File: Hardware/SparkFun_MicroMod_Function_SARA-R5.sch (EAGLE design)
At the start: 93 parts, among them J1 MICROMOD_FUNCTION_STANDARD, J2 U.FL, J4 U.FL, J9 NANO_SIM, Q2 310mA/60V/1.6Ω, Q3 310mA/60V/1.6Ω, Q5 310mA/60V/1.6Ω, Q6 310mA/60V/1.6Ω, U1 SARA-R510M8S, U11 74HC1G04, U2 SN74AVC4T774PW, U3 3.3V, U4 EEPROM, U5 AP7361C-33FGE

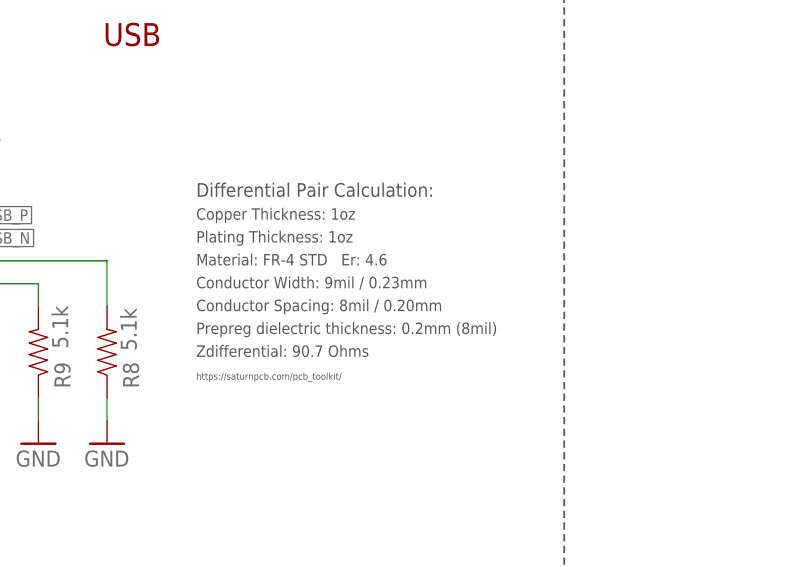
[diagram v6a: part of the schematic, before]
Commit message: USB lines updated for correct impedance calcs
-updated trace width and spacing to hit a 90 ohm differential impedance on D+/D-
-updated calculation text paragraph in SCH
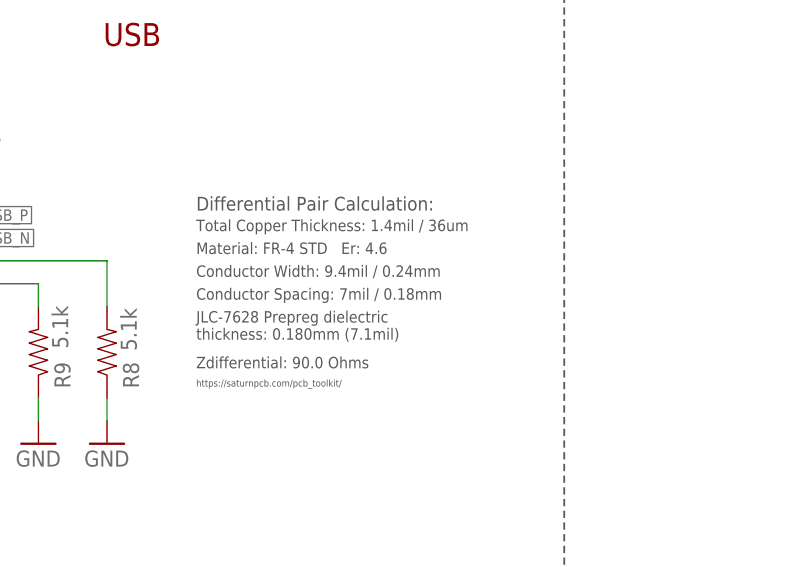
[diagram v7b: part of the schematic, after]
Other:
- note added: "Conductor Spacing: 7mil / 0.18mm"
- note added: "Conductor Width: 9.4mil / 0.24mm"
- note added: "JLC-7628 Prepreg dielectric thickness: 0.180mm (7.1mil)"
- note added: "Total Copper Thickness: 1.4mil / 36um"
- note added: "Zdifferential: 90.0 Ohms"
- note removed: "Conductor Spacing: 8mil / 0.20mm"
- note removed: "Conductor Width: 9mil / 0.23mm"
- note removed: "Copper Thickness: 1oz"
- note removed: "Plating Thickness: 1oz"
- note removed: "Prepreg dielectric thickness: 0.2mm (8mil)"
- note removed: "Zdifferential: 90.7 Ohms"
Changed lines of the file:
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@@
 <clearance class="3" value="0.1778"/>
 </class>
-<class number="4" name="DiffPair" width="0.2286" drill="0">
-<clearance class="4" value="0.2032"/>
+<class number="4" name="DiffPair" width="0.24" drill="0">
+<clearance class="4" value="0.1778"/>
 </class>
 </classes>
@@
 <text x="241.3" y="182.88" size="2.54" layer="97" font="vector">50Ω</text>
 <wire x1="330.2" y1="35.56" x2="330.2" y2="78.74" width="0.2032" layer="97" style="longdash"/>
-<text x="180.086" y="136.652" size="1.27" layer="97" font="vector">Plating Thickness: 1oz</text>
-<text x="180.086" y="134.112" size="1.27" layer="97" font="vector">Material: FR-4 STD   Er: 4.6</text>
-<text x="180.086" y="139.192" size="1.27" layer="97" font="vector">Copper Thickness: 1oz</text>
-<text x="180.086" y="129.032" size="1.27" layer="97" font="vector">Conductor Spacing: 8mil / 0.20mm</text>
-<text x="180.086" y="131.572" size="1.27" layer="97" font="vector">Conductor Width: 9mil / 0.23mm</text>
-<text x="180.086" y="126.492" size="1.27" layer="97" font="vector">Prepreg dielectric thickness: 0.2mm (8mil)</text>
-<text x="180.086" y="121.412" size="0.762" layer="97" font="vector">https://saturnpcb.com/pcb_toolkit/</text>
-<text x="180.086" y="141.732" size="1.524" layer="97" font="vector" ratio="15">Differential Pair Calculation:</text>
-<text x="180.086" y="123.952" size="1.27" layer="97" font="vector">Zdifferential: 90.7 Ohms</text>
+<text x="180.086" y="136.652" size="1.27" layer="97" font="vector"></text>
+<text x="180.086" y="136.652" size="1.27" layer="97" font="vector" align="top-left">Material: FR-4 STD   Er: 4.6</text>
+<text x="180.086" y="139.192" size="1.27" layer="97" font="vector" align="top-left">Total Copper Thickness: 1.4mil / 36um</text>
+<text x="180.086" y="131.572" size="1.27" layer="97" font="vector" align="top-left">Conductor Spacing: 7mil / 0.18mm</text>
+<text x="180.086" y="134.112" size="1.27" layer="97" font="vector" align="top-left">Conductor Width: 9.4mil / 0.24mm</text>
+<text x="180.086" y="129.032" size="1.27" layer="97" font="vector" align="top-left">JLC-7628 Prepreg dielectric
+thickness: 0.180mm (7.1mil)</text>
+<text x="180.086" y="121.412" size="0.762" layer="97" font="vector" align="top-left">https://saturnpcb.com/pcb_toolkit/</text>
+<text x="180.086" y="141.732" size="1.524" layer="97" font="vector" ratio="15" align="top-left">Differential Pair Calculation:</text>
+<text x="180.086" y="123.952" size="1.27" layer="97" font="vector" align="top-left">Zdifferential: 90.0 Ohms</text>
 <text x="139.7" y="88.9" size="2.032" layer="97" font="vector" rot="MR180" align="top-left">USB_SHLD Jumper
 Use this jumper to connect/disconnect

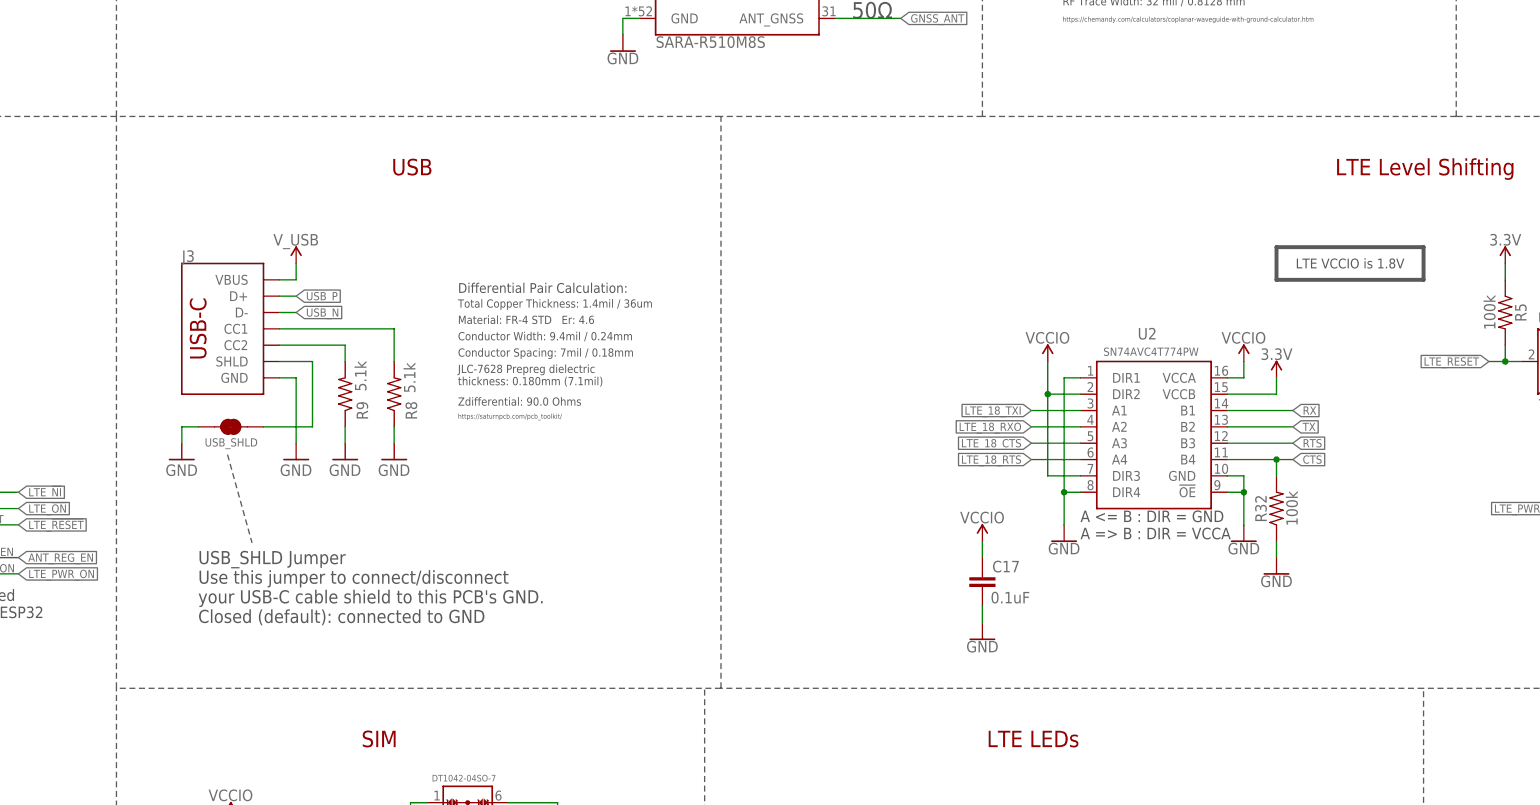
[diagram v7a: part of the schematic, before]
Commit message: ESD diode on D+ and D- USB lines
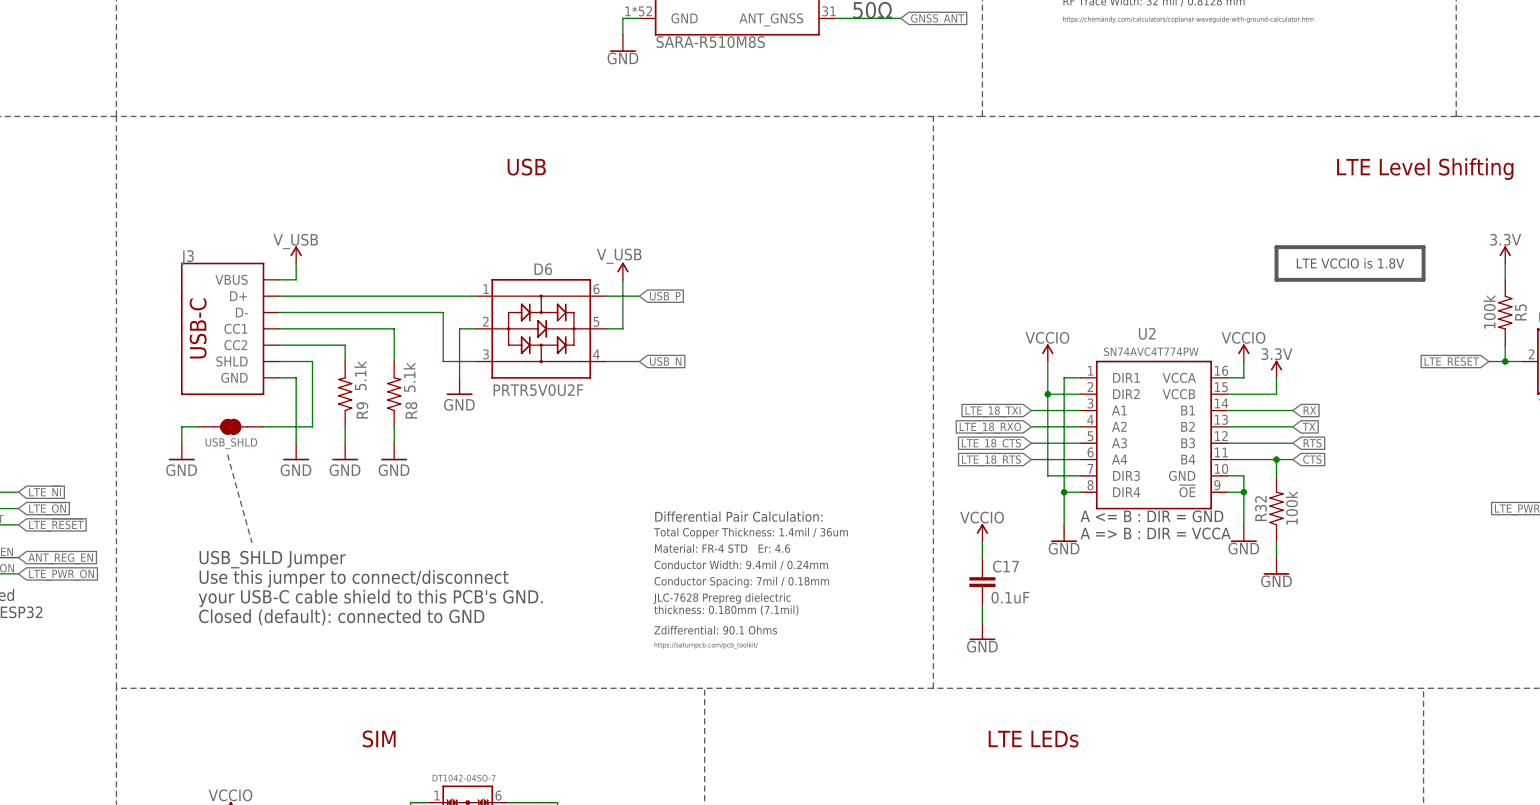
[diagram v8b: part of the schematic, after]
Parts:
- added D6: PRTR5V0U2F, SparkFun-IC-Power:PRTR5V0U2F
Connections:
- new net N$10: D6.1, J3.D+
- new net N$15: D6.3, J3.D-
- net GND: now also D6.2
- net USB_N: now also D6.4; no longer J3.D-
- net USB_P: now also D6.6; no longer J3.D+
- net V_USB: now also D6.5
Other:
- note added: "Zdifferential: 90.1 Ohms"
- note removed: "Zdifferential: 90.0 Ohms"
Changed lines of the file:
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@@
 <part name="GND25" library="SparkFun-PowerSymbols" deviceset="GND" device=""/>
 <part name="GND26" library="SparkFun-PowerSymbols" deviceset="GND" device=""/>
+<part name="GND27" library="SparkFun-PowerSymbols" deviceset="GND" device=""/>
+<part name="D6" library="SparkFun-IC-Power" deviceset="PRTR5V0U2" device="F"/>
+<part name="SUPPLY21" library="SparkFun-PowerSymbols" deviceset="V_USB" device=""/>
 </parts>
 <sheets>
@@
 <text x="274.066" y="182.372" size="0.762" layer="97" font="vector">https://chemandy.com/calculators/coplanar-waveguide-with-ground-calculator.htm</text>
 <text x="274.066" y="200.152" size="1.524" layer="97" font="vector" ratio="15">Microstrip Calculation:</text>
-<text x="172.974" y="159.766" size="2.54" layer="94" font="vector" align="center">USB</text>
+<text x="190.754" y="159.766" size="2.54" layer="94" font="vector" align="center">USB</text>
 <wire x1="431.8" y1="167.64" x2="335.28" y2="167.64" width="0.2032" layer="97" style="longdash"/>
 <wire x1="335.28" y1="167.64" x2="261.62" y2="167.64" width="0.2032" layer="97" style="longdash"/>
-<wire x1="261.62" y1="167.64" x2="220.98" y2="167.64" width="0.2032" layer="97" style="longdash"/>
-<wire x1="220.98" y1="167.64" x2="127" y2="167.64" width="0.2032" layer="97" style="longdash"/>
+<wire x1="261.62" y1="167.64" x2="254" y2="167.64" width="0.2032" layer="97" style="longdash"/>
+<wire x1="254" y1="167.64" x2="127" y2="167.64" width="0.2032" layer="97" style="longdash"/>
 <wire x1="431.8" y1="78.74" x2="330.2" y2="78.74" width="0.2032" layer="97" style="longdash"/>
-<wire x1="330.2" y1="78.74" x2="220.98" y2="78.74" width="0.2032" layer="97" style="longdash"/>
-<wire x1="220.98" y1="78.74" x2="127" y2="78.74" width="0.2032" layer="97" style="longdash"/>
+<wire x1="330.2" y1="78.74" x2="254" y2="78.74" width="0.2032" layer="97" style="longdash"/>
+<wire x1="254" y1="78.74" x2="127" y2="78.74" width="0.2032" layer="97" style="longdash"/>
 <wire x1="261.62" y1="167.64" x2="261.62" y2="279.4" width="0.2032" layer="97" style="longdash"/>
-<wire x1="220.98" y1="78.74" x2="220.98" y2="167.64" width="0.2032" layer="97" style="longdash"/>
+<wire x1="254" y1="78.74" x2="254" y2="167.64" width="0.2032" layer="97" style="longdash"/>
 <wire x1="218.44" y1="0" x2="218.44" y2="78.74" width="0.2032" layer="97" style="longdash"/>
 <text x="92.71" y="89.662" size="1.778" layer="97" font="vector">F6/F7 are shared
@@
 <wire x1="330.2" y1="35.56" x2="330.2" y2="78.74" width="0.2032" layer="97" style="longdash"/>
 <text x="180.086" y="136.652" size="1.27" layer="97" font="vector"></text>
-<text x="180.086" y="136.652" size="1.27" layer="97" font="vector" align="top-left">Material: FR-4 STD   Er: 4.6</text>
-<text x="180.086" y="139.192" size="1.27" layer="97" font="vector" align="top-left">Total Copper Thickness: 1.4mil / 36um</text>
-<text x="180.086" y="131.572" size="1.27" layer="97" font="vector" align="top-left">Conductor Spacing: 7mil / 0.18mm</text>
-<text x="180.086" y="134.112" size="1.27" layer="97" font="vector" align="top-left">Conductor Width: 9.4mil / 0.24mm</text>
-<text x="180.086" y="129.032" size="1.27" layer="97" font="vector" align="top-left">JLC-7628 Prepreg dielectric
+<text x="210.566" y="101.092" size="1.27" layer="97" font="vector" align="top-left">Material: FR-4 STD   Er: 4.6</text>
+<text x="210.566" y="103.632" size="1.27" layer="97" font="vector" align="top-left">Total Copper Thickness: 1.4mil / 36um</text>
+<text x="210.566" y="96.012" size="1.27" layer="97" font="vector" align="top-left">Conductor Spacing: 7mil / 0.18mm</text>
+<text x="210.566" y="98.552" size="1.27" layer="97" font="vector" align="top-left">Conductor Width: 9.4mil / 0.24mm</text>
+<text x="210.566" y="93.472" size="1.27" layer="97" font="vector" align="top-left">JLC-7628 Prepreg dielectric
 thickness: 0.180mm (7.1mil)</text>
-<text x="180.086" y="121.412" size="0.762" layer="97" font="vector" align="top-left">https://saturnpcb.com/pcb_toolkit/</text>
-<text x="180.086" y="141.732" size="1.524" layer="97" font="vector" ratio="15" align="top-left">Differential Pair Calculation:</text>
-<text x="180.086" y="123.952" size="1.27" layer="97" font="vector" align="top-left">Zdifferential: 90.0 Ohms</text>
+<text x="210.566" y="85.852" size="0.762" layer="97" font="vector" align="top-left">https://saturnpcb.com/pcb_toolkit/</text>
+<text x="210.566" y="106.172" size="1.524" layer="97" font="vector" ratio="15" align="top-left">Differential Pair Calculation:</text>
+<text x="210.566" y="88.392" size="1.27" layer="97" font="vector" align="top-left">Zdifferential: 90.1 Ohms</text>
 <text x="139.7" y="88.9" size="2.032" layer="97" font="vector" rot="MR180" align="top-left">USB_SHLD Jumper
 Use this jumper to connect/disconnect
@@
 <instance part="GND26" gate="1" x="154.94" y="114.3" smashed="yes">
 <attribute name="VALUE" x="152.4" y="111.76" size="1.778" layer="96" font="vector"/>
+</instance>
+<instance part="GND27" gate="1" x="180.34" y="124.46" smashed="yes">
+<attribute name="VALUE" x="177.8" y="121.92" size="1.778" layer="96" font="vector"/>
+</instance>
+<instance part="D6" gate="D1" x="193.04" y="134.62" smashed="yes">
+<attribute name="NAME" x="191.77" y="143.002" size="1.778" layer="95" font="vector"/>
+<attribute name="VALUE" x="185.42" y="125.984" size="1.778" layer="96" font="vector" align="top-left"/>
+</instance>
+<instance part="SUPPLY21" gate="G$1" x="205.74" y="142.24" smashed="yes">
+<attribute name="VALUE" x="201.676" y="145.288" size="1.778" layer="96" font="vector"/>
 </instance>
 </instances>
@@
 <wire x1="137.16" y1="119.38" x2="137.16" y2="116.84" width="0.1524" layer="91"/>
 </segment>
+<segment>
+<pinref part="GND27" gate="1" pin="GND"/>
+<wire x1="180.34" y1="134.62" x2="180.34" y2="127" width="0.1524" layer="91"/>
+<pinref part="D6" gate="D1" pin="2"/>
+<wire x1="180.34" y1="134.62" x2="182.88" y2="134.62" width="0.1524" layer="91"/>
+</segment>
 </net>
 <net name="EN" class="0">
@@
 <label x="205.74" y="215.9" size="1.27" layer="95" font="vector" rot="R180" xref="yes"/>
 <pinref part="U1" gate="G$2" pin="VUSB_DET"/>
+</segment>
+<segment>
+<pinref part="SUPPLY21" gate="G$1" pin="V_USB"/>
+<wire x1="203.2" y1="134.62" x2="205.74" y2="134.62" width="0.1524" layer="91"/>
+<wire x1="205.74" y1="134.62" x2="205.74" y2="142.24" width="0.1524" layer="91"/>
+<pinref part="D6" gate="D1" pin="5"/>
 </segment>
 </net>
@@
 <net name="USB_P" class="4">
 <segment>
-<pinref part="J3" gate="J1" pin="D+"/>
-<wire x1="152.4" y1="139.7" x2="154.94" y2="139.7" width="0.1524" layer="91"/>
-<label x="154.94" y="139.7" size="1.27" layer="95" font="vector" xref="yes"/>
-</segment>
-<segment>
 <wire x1="208.28" y1="187.96" x2="205.74" y2="187.96" width="0.1524" layer="91"/>
 <label x="205.74" y="187.96" size="1.27" layer="95" font="vector" rot="R180" xref="yes"/>
@@
 <label x="53.34" y="114.3" size="1.27" layer="95" font="vector" rot="R180" xref="yes"/>
 </segment>
+<segment>
+<label x="208.28" y="139.7" size="1.27" layer="95" font="vector" xref="yes"/>
+<wire x1="208.28" y1="139.7" x2="203.2" y2="139.7" width="0.1524" layer="91"/>
+<pinref part="D6" gate="D1" pin="6"/>
+</segment>
 </net>
 <net name="USB_N" class="4">
-<segment>
-<pinref part="J3" gate="J1" pin="D-"/>
-<wire x1="152.4" y1="137.16" x2="154.94" y2="137.16" width="0.1524" layer="91"/>
-<label x="154.94" y="137.16" size="1.27" layer="95" font="vector" xref="yes"/>
-</segment>
 <segment>
 <wire x1="208.28" y1="190.5" x2="205.74" y2="190.5" width="0.1524" layer="91"/>
@@
 <wire x1="55.88" y1="116.84" x2="53.34" y2="116.84" width="0.1524" layer="91"/>
 <label x="53.34" y="116.84" size="1.27" layer="95" font="vector" rot="R180" xref="yes"/>
+</segment>
+<segment>
+<label x="208.28" y="129.54" size="1.27" layer="95" font="vector" xref="yes"/>
+<wire x1="208.28" y1="129.54" x2="203.2" y2="129.54" width="0.1524" layer="91"/>
+<pinref part="D6" gate="D1" pin="4"/>
 </segment>
 </net>
@@
 </segment>
 </net>
+<net name="N$15" class="4">
+<segment>
+<pinref part="J3" gate="J1" pin="D-"/>
+<wire x1="152.4" y1="137.16" x2="177.8" y2="137.16" width="0.1524" layer="91"/>
+<wire x1="177.8" y1="137.16" x2="177.8" y2="129.54" width="0.1524" layer="91"/>
+<pinref part="D6" gate="D1" pin="3"/>
+<wire x1="177.8" y1="129.54" x2="182.88" y2="129.54" width="0.1524" layer="91"/>
+</segment>
+</net>
+<net name="N$10" class="0">
+<segment>
+<pinref part="J3" gate="J1" pin="D+"/>
+<pinref part="D6" gate="D1" pin="1"/>
+<wire x1="152.4" y1="139.7" x2="182.88" y2="139.7" width="0.1524" layer="91"/>
+</segment>
+</net>
